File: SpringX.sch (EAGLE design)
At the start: 9 parts, among them U1 MCP1703-5002E/CB, U2 MCP602ST

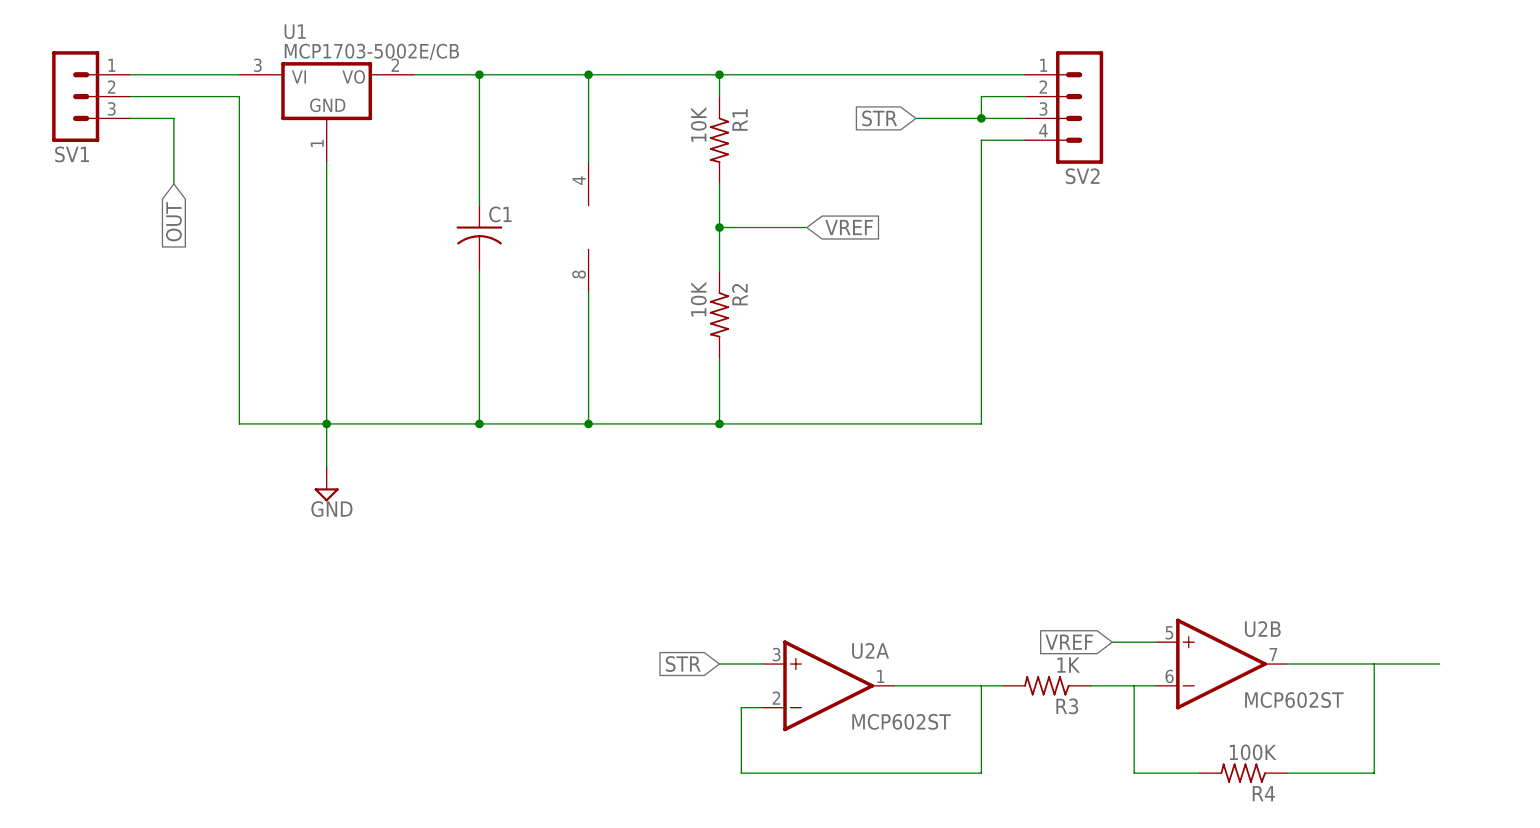
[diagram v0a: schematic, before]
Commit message: Revised board layout to use solder pads for strain gauges and Molex PICO-SPOX connector for car interface.
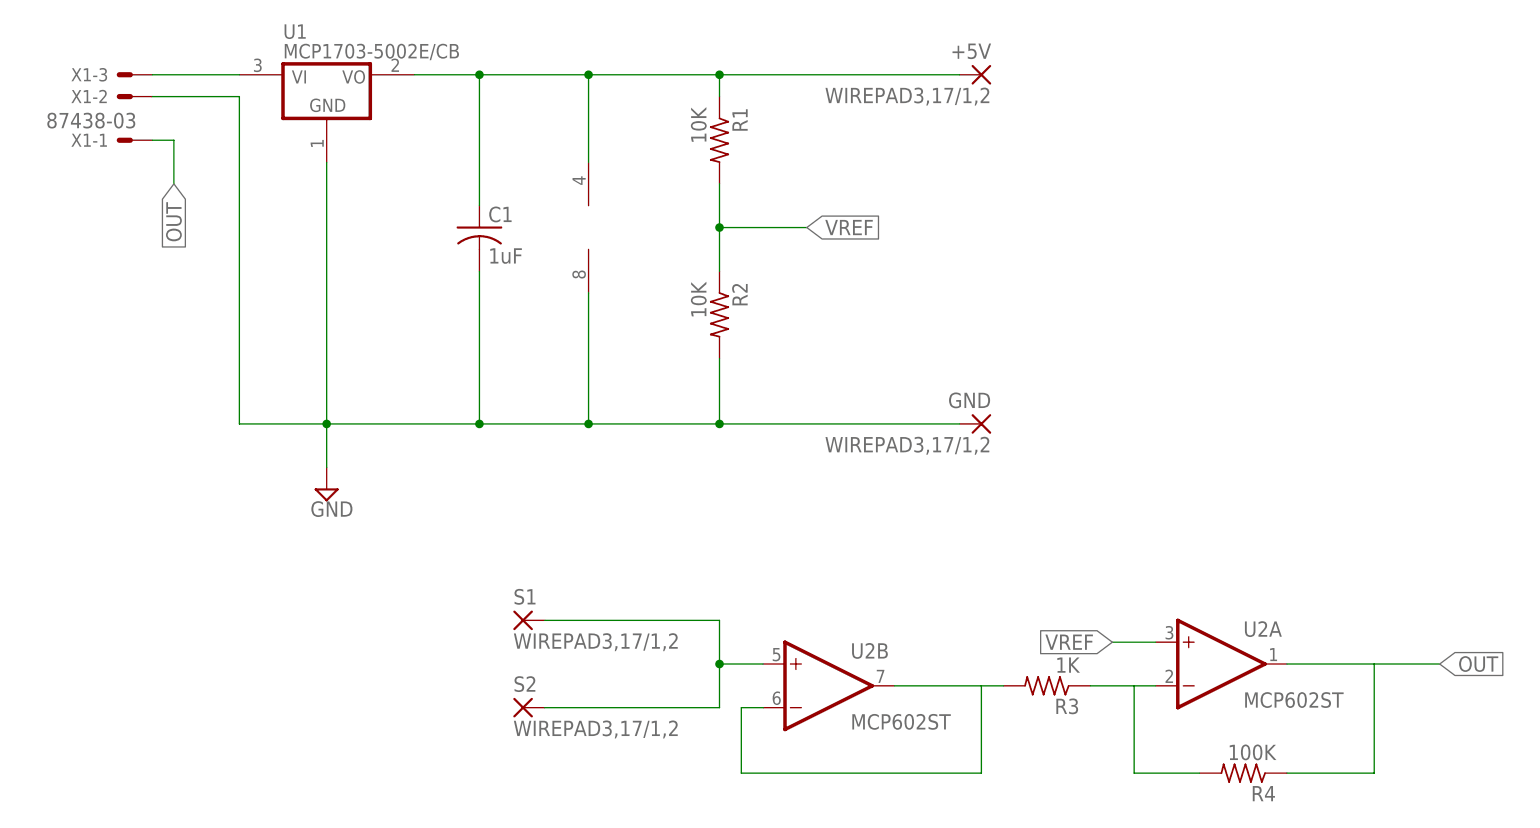
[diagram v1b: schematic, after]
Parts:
- removed SV1: (no value), con-lstb:MA03-1
- removed SV2: (no value), con-lstb:MA04-1
- added +5V, GND, S1, S2: WIREPAD3,17/1,2, wirepad:WIREPAD3,17/1,2
- added X1: 87438-03, con-molex:87438-03
- C1: value (none) -> 1uF
- R1, R2, R3, R4: device resistor:R-US_R0603 -> rcl:R-US_R0603
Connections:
- net 5V: now also +5V.P; no longer SV2.1
- net GND: now also GND.P, X1-2.S; no longer SV1.2, SV2.4
- net N$1: now also X1-3.S; no longer SV1.1
- net N$2: now also U2B.-IN, U2B.OUT; no longer U2A.-IN, U2A.OUT
- net N$4: now also U2A.-IN; no longer U2B.-IN
- net OUT: now also U2A.OUT, X1-1.S; no longer SV1.3, U2B.OUT
- net STR: now also S1.P, S2.P, U2B.+IN; no longer SV2.2, SV2.3, U2A.+IN
- net VREF: now also U2A.+IN; no longer U2B.+IN
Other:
- moved on the sheet: U2A, U2B
